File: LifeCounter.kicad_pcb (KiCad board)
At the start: 4 copper layers, 132.3 x 43.9 mm, 44 parts, among them IC2 AP3012KTR-E1, IC3 MCP73831T-2ATI_OT, IC4 AP2112K-3.3TRG1, IC5 STM32H562VGT6, J1 54104-4531, J2 USB_C_Receptacle_USB2.0_14P, Q1 AO3401A

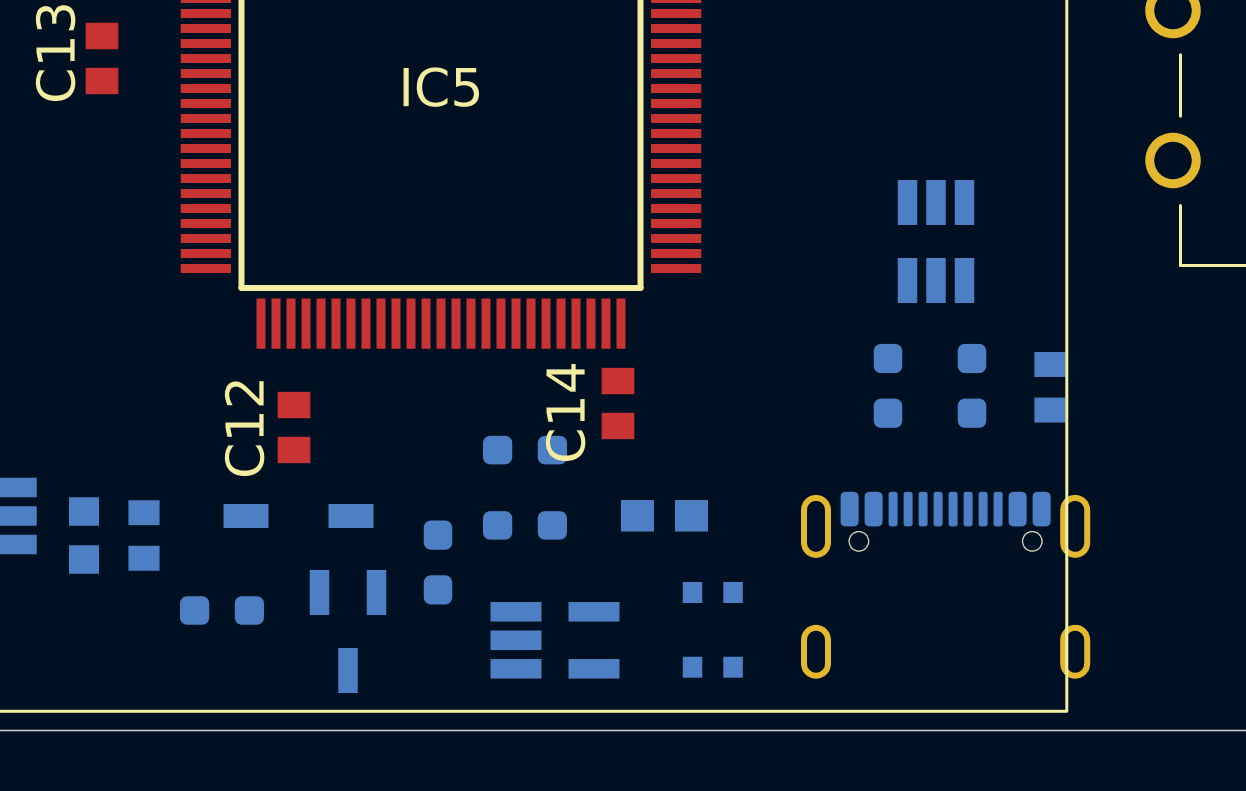
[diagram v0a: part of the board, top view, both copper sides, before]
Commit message: added a ferride bead, added a 100nF filtering cap to the mosfet gate and changed the resistor pulldown value from 100k to 1k, removed the 1k resistor in series at the gate pin
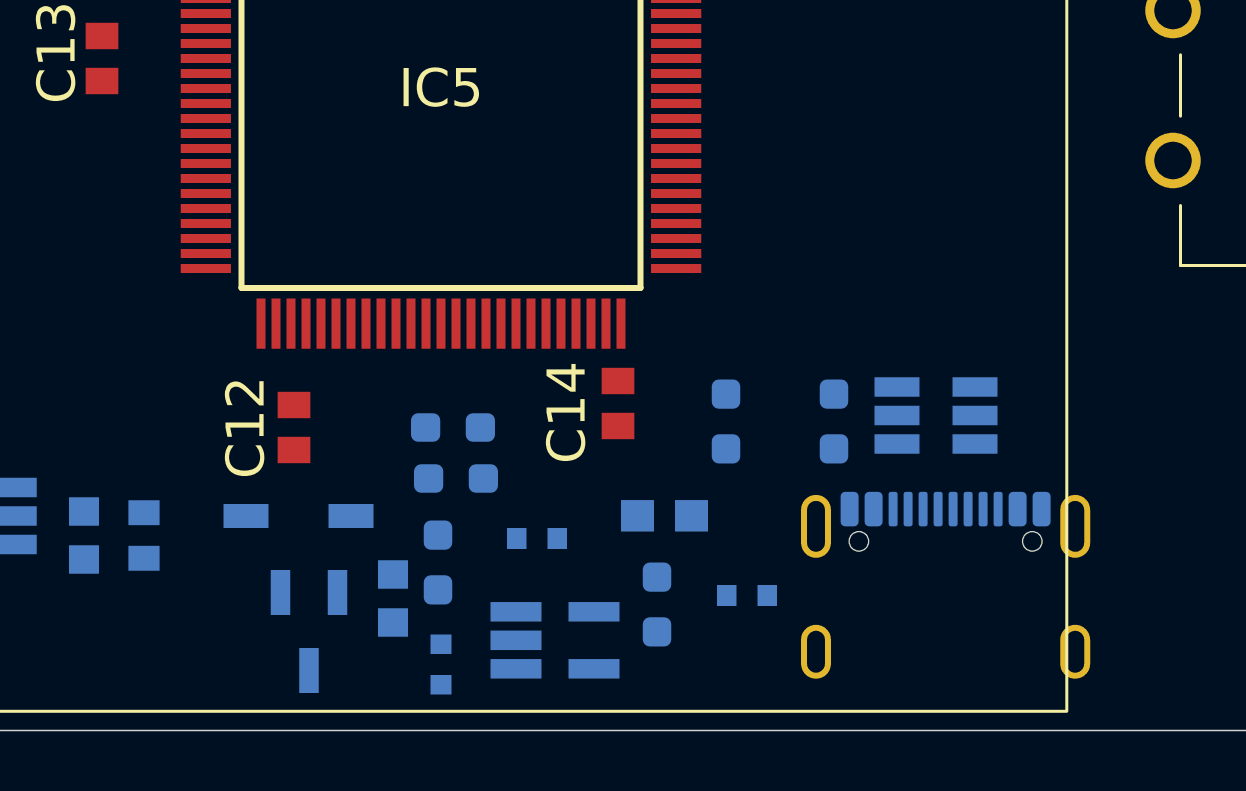
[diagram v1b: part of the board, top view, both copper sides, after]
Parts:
- removed R6: 100k, Resistor_SMD:R_0603_1608Metric_Pad0.98x0.95mm_HandSolder
- added FB1: BLM18EG221TN1D, LifeCounter-Footprints:Murata_BLM18EG101TH1D, B.Cu at (174.1, 102.8)
- added R8: 2, Resistor_SMD:R_0603_1608Metric_Pad0.98x0.95mm_HandSolder, B.Cu at (181.3, 100.8)
- C4: value 10uF -> 100nF; footprint LifeCounter-Footprints:Samsung_CAPC1608X90M -> LifeCounter-Footprints:Kemet_C0603
- moved C4 23.0 mm to (172.5, 100.6), turned to -90 degrees
- moved R3 8.29 mm to (183.6, 94.7)
- moved C5 7.26 mm to (177.3, 98.6), turned to 180 degrees
- moved D2 5.80 mm to (190.6, 94.5), turned to 0 degrees
- moved R4 2.78 mm to (174.6, 96.6)
- moved R5 2.52 mm to (174.5, 94.9)
- moved R2 2.16 mm to (187.2, 94.7)
- moved Q1 1.30 mm to (169.7, 101.7)
- moved C6 1.14 mm to (184.3, 100.5)
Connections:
- C6 pad 1: /Power_Management/VBUS -> Net-(C6-Pad1)
- Q1 pad 1: Net-(Q1-G) -> /Power_Management/VBUS
- Q1 pad 2: /Power_Management/BAT+ -> Net-(D4-K)
- Q1 pad 3: Net-(D4-K) -> Net-(Q1-D)
- R7 pad 1: Net-(Q1-G) -> GND
